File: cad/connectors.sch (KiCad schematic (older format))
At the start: 18 parts, among them J201 JACK_IN, J202 JACK_OUT, J203 CONN_PSU, J204 SW_BYPASS, J206 SW_FAT, K201 TQ2SA-5V, Q201 DTC123Y, U201 4013

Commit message: Placed components. Added possibility of having switches on connector board or circuit board.
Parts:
- added R204, R205: 150, Resistors_SMD:R_0805, symbol R
- C202: renamed from C?; value CP -> 10u; footprint (none) -> Capacitors_SMD:CP_Elec_4x4.5
- J205: renamed from J206; value SW_FAT -> SW_FAT_A; footprint Pin_Headers:Pin_Header_Straight_1x03_Pitch2.54mm -> flax_lib:SW_SPDT_through_hole
- J206: renamed from J?; footprint (none) -> flax_lib:SW_DPDT_through_hole
- J207, J208: renamed from J?; footprint (none) -> Pin_Headers:Pin_Header_Straight_1x06_Pitch2.54mm
- gave numbers to parts that had none: 1
- renumbered C201 to C203
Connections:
- wire segments 77 -> 79
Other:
- moved on the sheet: Q201
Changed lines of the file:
@@
 L DTC123Y Q201
 U 1 1 599C9C32
-P 5800 3800
-F 0 "Q201" H 6000 3875 50  0000 L CNN
-F 1 "DTC123Y" H 6000 3800 50  0000 L CNN
-F 2 "TO_SOT_Packages_SMD:SOT-23" H 5800 3800 50  0001 L CNN
-F 3 "" H 5800 3800 50  0001 L CNN
-	1    5800 3800
+P 5800 4200
+F 0 "Q201" H 6000 4275 50  0000 L CNN
+F 1 "DTC123Y" H 6000 4200 50  0000 L CNN
+F 2 "TO_SOT_Packages_SMD:SOT-23" H 5800 4200 50  0001 L CNN
+F 3 "" H 5800 4200 50  0001 L CNN
+	1    5800 4200
 	1    0    0    -1
 $EndComp
@@
 $EndComp
 $Comp
-L C C201
+L C C203
 U 1 1 599C9FED
 P 9800 950
-F 0 "C201" H 9825 1050 50  0000 L CNN
+F 0 "C203" H 9825 1050 50  0000 L CNN
 F 1 "100n" H 9825 850 50  0000 L CNN
 F 2 "Capacitors_SMD:C_0603" H 9838 800 50  0001 C CNN
@@
 $EndComp
 $Comp
-L GND #PWR218
+L GND #PWR01
 U 1 1 599D227D
 P 10400 2700
-F 0 "#PWR218" H 10400 2450 50  0001 C CNN
+F 0 "#PWR01" H 10400 2450 50  0001 C CNN
 F 1 "GND" H 10400 2550 50  0000 C CNN
 F 2 "" H 10400 2700 50  0001 C CNN
@@
 FX_OUT_A
 $Comp
-L VDD #PWR217
+L VDD #PWR02
 U 1 1 599D577B
 P 10400 2000
-F 0 "#PWR217" H 10400 1850 50  0001 C CNN
+F 0 "#PWR02" H 10400 1850 50  0001 C CNN
 F 1 "VDD" H 10400 2150 50  0000 C CNN
 F 2 "" H 10400 2000 50  0001 C CNN
@@
 $EndComp
 $Comp
-L VDD #PWR205
+L VDD #PWR03
 U 1 1 599D5C70
 P 1700 3900
-F 0 "#PWR205" H 1700 3750 50  0001 C CNN
+F 0 "#PWR03" H 1700 3750 50  0001 C CNN
 F 1 "VDD" H 1700 4050 50  0000 C CNN
 F 2 "" H 1700 3900 50  0001 C CNN
@@
 $EndComp
 $Comp
-L VSS #PWR201
+L VSS #PWR04
 U 1 1 599D5CD2
 P 1700 1100
-F 0 "#PWR201" H 1700 950 50  0001 C CNN
+F 0 "#PWR04" H 1700 950 50  0001 C CNN
 F 1 "VSS" H 1700 1250 50  0000 C CNN
 F 2 "" H 1700 1100 50  0001 C CNN
@@
 $EndComp
 $Comp
-L VDD #PWR215
+L VDD #PWR05
 U 1 1 599D63BF
 P 9800 700
-F 0 "#PWR215" H 9800 550 50  0001 C CNN
+F 0 "#PWR05" H 9800 550 50  0001 C CNN
 F 1 "VDD" H 9800 850 50  0000 C CNN
 F 2 "" H 9800 700 50  0001 C CNN
@@
 NoConn ~ 9400 1600
 $Comp
-L VSS #PWR216
+L VSS #PWR06
 U 1 1 599D692C
 P 9800 1200
-F 0 "#PWR216" H 9800 1050 50  0001 C CNN
+F 0 "#PWR06" H 9800 1050 50  0001 C CNN
 F 1 "VSS" H 9800 1350 50  0000 C CNN
 F 2 "" H 9800 1200 50  0001 C CNN
@@
 $EndComp
 $Comp
-L VSS #PWR213
+L VSS #PWR07
 U 1 1 599D6A53
 P 8800 800
-F 0 "#PWR213" H 8800 650 50  0001 C CNN
+F 0 "#PWR07" H 8800 650 50  0001 C CNN
 F 1 "VSS" H 8800 950 50  0000 C CNN
 F 2 "" H 8800 800 50  0001 C CNN
@@
 $EndComp
 $Comp
-L VDD #PWR214
+L VDD #PWR08
 U 1 1 599D6F63
 P 8800 2000
-F 0 "#PWR214" H 8800 1850 50  0001 C CNN
+F 0 "#PWR08" H 8800 1850 50  0001 C CNN
 F 1 "VDD" H 8800 2150 50  0000 C CNN
 F 2 "" H 8800 2000 50  0001 C CNN
@@
 NoConn ~ 8200 1200
 $Comp
-L VSS #PWR210
+L VSS #PWR09
 U 1 1 599DA718
 P 5700 800
-F 0 "#PWR210" H 5700 650 50  0001 C CNN
+F 0 "#PWR09" H 5700 650 50  0001 C CNN
 F 1 "VSS" H 5700 950 50  0000 C CNN
 F 2 "" H 5700 800 50  0001 C CNN
@@
 $EndComp
 $Comp
-L VSS #PWR211
+L VSS #PWR010
 U 1 1 599DA798
 P 5700 2000
-F 0 "#PWR211" H 5700 1850 50  0001 C CNN
+F 0 "#PWR010" H 5700 1850 50  0001 C CNN
 F 1 "VSS" H 5700 2150 50  0000 C CNN
 F 2 "" H 5700 2000 50  0001 C CNN
@@
 $EndComp
 $Comp
-L VSS #PWR208
+L VSS #PWR011
 U 1 1 599DB73B
 P 4900 2000
-F 0 "#PWR208" H 4900 1850 50  0001 C CNN
+F 0 "#PWR011" H 4900 1850 50  0001 C CNN
 F 1 "VSS" H 4900 2150 50  0000 C CNN
 F 2 "" H 4900 2000 50  0001 C CNN
@@
 $EndComp
 $Comp
-L VDD #PWR207
+L VDD #PWR012
 U 1 1 599DB9B0
 P 4200 1400
-F 0 "#PWR207" H 4200 1250 50  0001 C CNN
+F 0 "#PWR012" H 4200 1250 50  0001 C CNN
 F 1 "VDD" H 4200 1550 50  0000 C CNN
 F 2 "" H 4200 1400 50  0001 C CNN
@@
 Text Label 6400 1200 0    60   ~ 0
 BYPASS_CMD
-Text Label 5400 3800 2    60   ~ 0
+Text Label 5400 4200 2    60   ~ 0
 BYPASS_CMD
 Text Label 10300 2600 2    60   ~ 0
 BYPASS_CMD
 $Comp
-L +BATT #PWR209
+L +BATT #PWR013
 U 1 1 599DDDBD
-P 5500 3000
-F 0 "#PWR209" H 5500 2850 50  0001 C CNN
-F 1 "+BATT" H 5500 3140 50  0000 C CNN
-F 2 "" H 5500 3000 50  0001 C CNN
-F 3 "" H 5500 3000 50  0001 C CNN
-	1    5500 3000
+P 4900 3000
+F 0 "#PWR013" H 4900 2850 50  0001 C CNN
+F 1 "+BATT" H 4900 3140 50  0000 C CNN
+F 2 "" H 4900 3000 50  0001 C CNN
+F 3 "" H 4900 3000 50  0001 C CNN
+	1    4900 3000
 	0    -1   -1   0
 $EndComp
@@
 AUDIO_OUT
 $Comp
-L CONN_01X03 J206
+L CONN_01X03 J205
 U 1 1 599E0F67
 P 8000 2700
-F 0 "J206" H 8000 2900 50  0000 C CNN
-F 1 "SW_FAT" V 8100 2700 50  0000 C CNN
-F 2 "Pin_Headers:Pin_Header_Straight_1x03_Pitch2.54mm" H 8000 2700 50  0001 C CNN
+F 0 "J205" H 8000 2900 50  0000 C CNN
+F 1 "SW_FAT_A" V 8100 2700 50  0000 C CNN
+F 2 "flax_lib:SW_SPDT_through_hole" H 8000 2700 50  0001 C CNN
 F 3 "" H 8000 2700 50  0001 C CNN
 	1    8000 2700
@@
 NoConn ~ 1600 2300
 $Comp
-L +BATT #PWR204
+L +BATT #PWR014
 U 1 1 599E2D1E
 P 1700 3800
-F 0 "#PWR204" H 1700 3650 50  0001 C CNN
+F 0 "#PWR014" H 1700 3650 50  0001 C CNN
 F 1 "+BATT" H 1700 3940 50  0000 C CNN
 F 2 "" H 1700 3800 50  0001 C CNN
@@
 $EndComp
 $Comp
-L VSS #PWR212
+L VSS #PWR015
 U 1 1 599E3B90
-P 5900 4100
-F 0 "#PWR212" H 5900 3950 50  0001 C CNN
-F 1 "VSS" H 5900 4250 50  0000 C CNN
-F 2 "" H 5900 4100 50  0001 C CNN
-F 3 "" H 5900 4100 50  0001 C CNN
-	1    5900 4100
+P 5900 4500
+F 0 "#PWR015" H 5900 4350 50  0001 C CNN
+F 1 "VSS" H 5900 4650 50  0000 C CNN
+F 2 "" H 5900 4500 50  0001 C CNN
+F 3 "" H 5900 4500 50  0001 C CNN
+	1    5900 4500
 	-1   0    0    1
 $EndComp
@@
 NoConn ~ 1600 1200
 $Comp
-L VSS #PWR202
+L VSS #PWR016
 U 1 1 599E4020
 P 1700 1900
-F 0 "#PWR202" H 1700 1750 50  0001 C CNN
+F 0 "#PWR016" H 1700 1750 50  0001 C CNN
 F 1 "VSS" H 1700 2050 50  0000 C CNN
 F 2 "" H 1700 1900 50  0001 C CNN
@@
 $EndComp
 $Comp
-L VSS #PWR203
+L VSS #PWR017
 U 1 1 599E457A
 P 1700 3700
-F 0 "#PWR203" H 1700 3550 50  0001 C CNN
+F 0 "#PWR017" H 1700 3550 50  0001 C CNN
 F 1 "VSS" H 1700 3850 50  0000 C CNN
 F 2 "" H 1700 3700 50  0001 C CNN
@@
 Connection ~ 5900 3500
 Wire Wire Line
-	5900 4000 5900 4100
-Wire Wire Line
-	5550 3800 4800 3800
+	5900 4400 5900 4500
+Wire Wire Line
+	5550 4200 4800 4200
 Wire Wire Line
 	6400 1600 6300 1600
@@
 	6300 1200 7000 1200
 Wire Wire Line
-	5500 3000 5700 3000
+	5300 3000 5700 3000
 Wire Wire Line
 	5700 3000 5700 3100
@@
 	2200 1300 2200 1400
 $Comp
-L VSS #PWR206
+L VSS #PWR018
 U 1 1 59A2E46C
 P 2200 1800
-F 0 "#PWR206" H 2200 1650 50  0001 C CNN
+F 0 "#PWR018" H 2200 1650 50  0001 C CNN
 F 1 "VSS" H 2200 1950 50  0000 C CNN
 F 2 "" H 2200 1800 50  0001 C CNN
@@
 Connection ~ 1650 1900
 $Comp
-L C C?
+L C C201
 U 1 1 59A4C299
 P 7650 2500
-F 0 "C?" H 7675 2600 50  0000 L CNN
+F 0 "C201" H 7675 2600 50  0000 L CNN
 F 1 "100n" H 7675 2400 50  0000 L CNN
 F 2 "Capacitors_SMD:C_0603" H 7688 2350 50  0001 C CNN
@@
 	7400 2500 7500 2500
 $Comp
-L CP C?
+L CP C202
 U 1 1 59A4C4B8
 P 7650 2900
-F 0 "C?" H 7675 3000 50  0000 L CNN
-F 1 "CP" H 7675 2800 50  0000 L CNN
-F 2 "" H 7688 2750 50  0001 C CNN
+F 0 "C202" H 7675 3000 50  0000 L CNN
+F 1 "10u" H 7675 2800 50  0000 L CNN
+F 2 "Capacitors_SMD:CP_Elec_4x4.5" H 7688 2750 50  0001 C CNN
 F 3 "" H 7650 2900 50  0001 C CNN
 	1    7650 2900
@@
 FX_IN_A
 $Comp
-L CONN_01X06 J?
+L CONN_01X06 J207
 U 1 1 59A4F4ED
 P 10700 2350
-F 0 "J?" H 10700 2700 50  0000 C CNN
+F 0 "J207" H 10700 2700 50  0000 C CNN
 F 1 "CONN_SIGNALS_A" V 10800 2350 50  0000 C CNN
-F 2 "" H 10700 2350 50  0001 C CNN
+F 2 "Pin_Headers:Pin_Header_Straight_1x06_Pitch2.54mm" H 10700 2350 50  0001 C CNN
 F 3 "" H 10700 2350 50  0001 C CNN
 	1    10700 2350
@@
 EQ_SW_1_1B
 $Comp
-L CONN_01X06 J?
+L CONN_01X06 J208
 U 1 1 59A529D0
 P 10700 3450
-F 0 "J?" H 10700 3800 50  0000 C CNN
+F 0 "J208" H 10700 3800 50  0000 C CNN
 F 1 "CONN_SW_EQ_A" V 10800 3450 50  0000 C CNN
-F 2 "" H 10700 3450 50  0001 C CNN
+F 2 "Pin_Headers:Pin_Header_Straight_1x06_Pitch2.54mm" H 10700 3450 50  0001 C CNN
 F 3 "" H 10700 3450 50  0001 C CNN
 	1    10700 3450
@@
 	9700 3700 10500 3700
 $Comp
-L CONN_02X03 J?
+L CONN_02X03 J206
 U 1 1 59A53228
 P 8050 3700
-F 0 "J?" H 8050 3900 50  0000 C CNN
+F 0 "J206" H 8050 3900 50  0000 C CNN
 F 1 "SW_EQ_A" H 8050 3500 50  0000 C CNN
-F 2 "" H 8050 2500 50  0001 C CNN
+F 2 "flax_lib:SW_DPDT_through_hole" H 8050 2500 50  0001 C CNN
 F 3 "" H 8050 2500 50  0001 C CNN
 	1    8050 3700
@@
 Wire Wire Line
 	8300 3800 9000 3800
+$Comp
+L R R204
+U 1 1 59A553B7
+P 5150 3000
+F 0 "R204" V 5230 3000 50  0000 C CNN
+F 1 "150" V 5150 3000 50  0000 C CNN
+F 2 "Resistors_SMD:R_0805" V 5080 3000 50  0001 C CNN
+F 3 "" H 5150 3000 50  0001 C CNN
+	1    5150 3000
+	0    -1   -1   0
+$EndComp
+Wire Wire Line
+	5000 3000 4900 3000
+$Comp
+L R R205
+U 1 1 59A55A74
+P 5900 3750
+F 0 "R205" V 5980 3750 50  0000 C CNN
+F 1 "150" V 5900 3750 50  0000 C CNN
+F 2 "Resistors_SMD:R_0805" V 5830 3750 50  0001 C CNN
+F 3 "" H 5900 3750 50  0001 C CNN
+	1    5900 3750
+	1    0    0    -1
+$EndComp
+Wire Wire Line
+	5900 3900 5900 4000
 $EndSCHEMATC

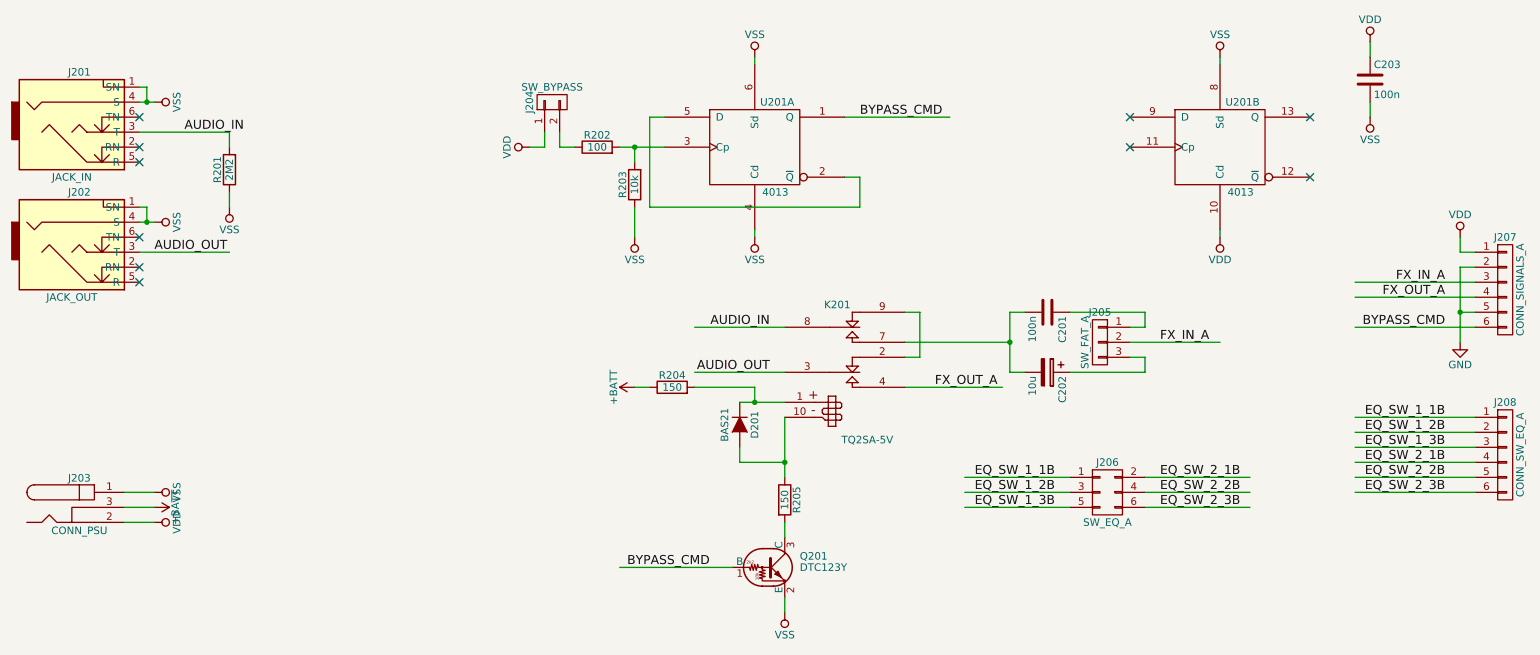
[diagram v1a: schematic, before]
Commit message: Corrected pots orientation.
Finished layout.
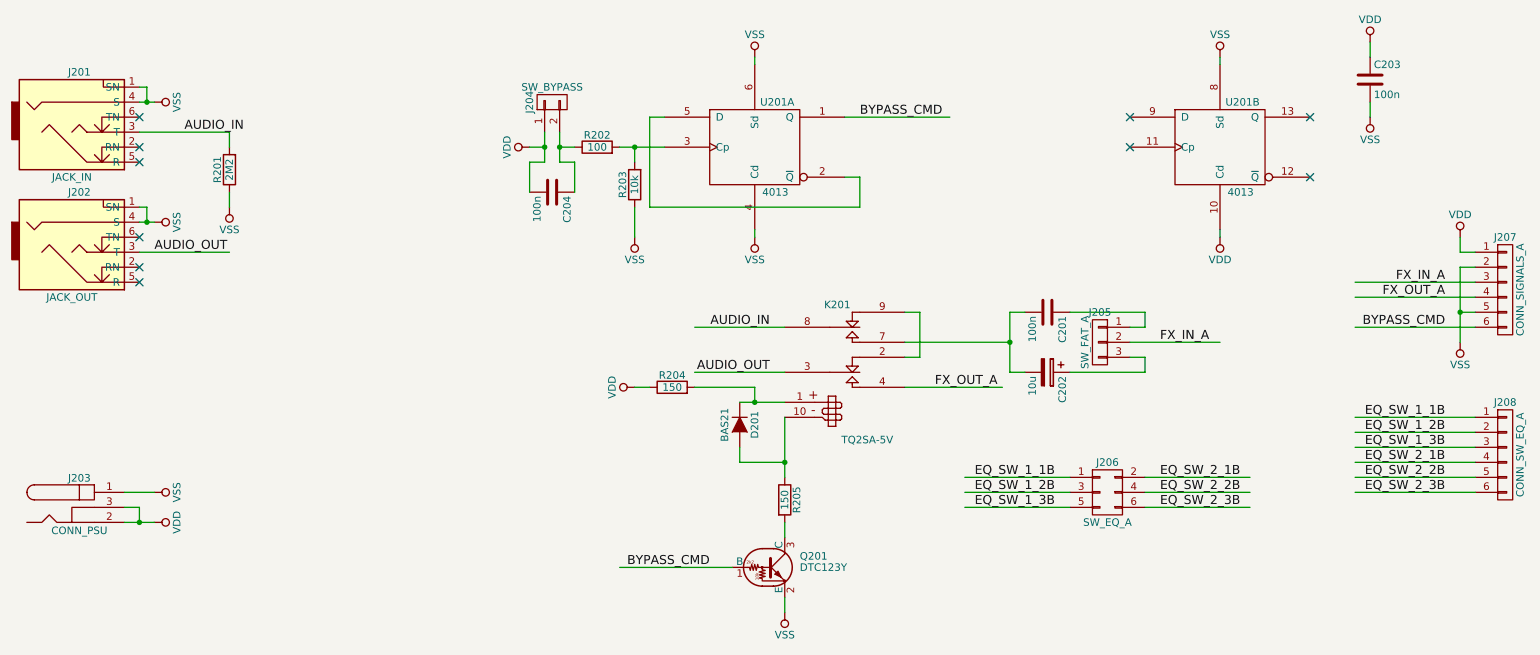
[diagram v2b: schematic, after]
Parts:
- added C204: 100n, Capacitors_SMD:C_0603, symbol C
- J207, J208: footprint Pin_Headers:Pin_Header_Straight_1x06_Pitch2.54mm -> Pin_Headers:Pin_Header_Straight_1x06_Pitch1.27mm
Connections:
- net labels removed: +BATT, GND
- wire segments 79 -> 84
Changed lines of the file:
@@
 LIBS:contrib
 LIBS:valves
-LIBS:flax_lib
 LIBS:hot_silicon_fuzz-cache
 EELAYER 25 0
@@
 	1    0    0    -1
 $EndComp
-$Comp
-L GND #PWR01
-U 1 1 599D227D
-P 10400 2700
-F 0 "#PWR01" H 10400 2450 50  0001 C CNN
-F 1 "GND" H 10400 2550 50  0000 C CNN
-F 2 "" H 10400 2700 50  0001 C CNN
-F 3 "" H 10400 2700 50  0001 C CNN
-	1    10400 2700
-	1    0    0    -1
-$EndComp
 Text Label 10300 2400 2    60   ~ 0
 FX_OUT_A
 $Comp
-L VDD #PWR02
+L VDD #PWR01
 U 1 1 599D577B
 P 10400 2000
-F 0 "#PWR02" H 10400 1850 50  0001 C CNN
+F 0 "#PWR01" H 10400 1850 50  0001 C CNN
 F 1 "VDD" H 10400 2150 50  0000 C CNN
 F 2 "" H 10400 2000 50  0001 C CNN
@@
 $EndComp
 $Comp
-L VDD #PWR03
+L VDD #PWR02
 U 1 1 599D5C70
 P 1700 3900
-F 0 "#PWR03" H 1700 3750 50  0001 C CNN
+F 0 "#PWR02" H 1700 3750 50  0001 C CNN
 F 1 "VDD" H 1700 4050 50  0000 C CNN
 F 2 "" H 1700 3900 50  0001 C CNN
@@
 $EndComp
 $Comp
-L VSS #PWR04
+L VSS #PWR03
 U 1 1 599D5CD2
 P 1700 1100
-F 0 "#PWR04" H 1700 950 50  0001 C CNN
+F 0 "#PWR03" H 1700 950 50  0001 C CNN
 F 1 "VSS" H 1700 1250 50  0000 C CNN
 F 2 "" H 1700 1100 50  0001 C CNN
@@
 $EndComp
 $Comp
-L VDD #PWR05
+L VDD #PWR04
 U 1 1 599D63BF
 P 9800 700
-F 0 "#PWR05" H 9800 550 50  0001 C CNN
+F 0 "#PWR04" H 9800 550 50  0001 C CNN
 F 1 "VDD" H 9800 850 50  0000 C CNN
 F 2 "" H 9800 700 50  0001 C CNN
@@
 NoConn ~ 9400 1600
 $Comp
-L VSS #PWR06
+L VSS #PWR05
 U 1 1 599D692C
 P 9800 1200
-F 0 "#PWR06" H 9800 1050 50  0001 C CNN
+F 0 "#PWR05" H 9800 1050 50  0001 C CNN
 F 1 "VSS" H 9800 1350 50  0000 C CNN
 F 2 "" H 9800 1200 50  0001 C CNN
@@
 $EndComp
 $Comp
-L VSS #PWR07
+L VSS #PWR06
 U 1 1 599D6A53
 P 8800 800
-F 0 "#PWR07" H 8800 650 50  0001 C CNN
+F 0 "#PWR06" H 8800 650 50  0001 C CNN
 F 1 "VSS" H 8800 950 50  0000 C CNN
 F 2 "" H 8800 800 50  0001 C CNN
@@
 $EndComp
 $Comp
-L VDD #PWR08
+L VDD #PWR07
 U 1 1 599D6F63
 P 8800 2000
-F 0 "#PWR08" H 8800 1850 50  0001 C CNN
+F 0 "#PWR07" H 8800 1850 50  0001 C CNN
 F 1 "VDD" H 8800 2150 50  0000 C CNN
 F 2 "" H 8800 2000 50  0001 C CNN
@@
 NoConn ~ 8200 1200
 $Comp
-L VSS #PWR09
+L VSS #PWR08
 U 1 1 599DA718
 P 5700 800
-F 0 "#PWR09" H 5700 650 50  0001 C CNN
+F 0 "#PWR08" H 5700 650 50  0001 C CNN
 F 1 "VSS" H 5700 950 50  0000 C CNN
 F 2 "" H 5700 800 50  0001 C CNN
@@
 $EndComp
 $Comp
-L VSS #PWR010
+L VSS #PWR09
 U 1 1 599DA798
 P 5700 2000
-F 0 "#PWR010" H 5700 1850 50  0001 C CNN
+F 0 "#PWR09" H 5700 1850 50  0001 C CNN
 F 1 "VSS" H 5700 2150 50  0000 C CNN
 F 2 "" H 5700 2000 50  0001 C CNN
@@
 $EndComp
 $Comp
-L VSS #PWR011
+L VSS #PWR010
 U 1 1 599DB73B
 P 4900 2000
-F 0 "#PWR011" H 4900 1850 50  0001 C CNN
+F 0 "#PWR010" H 4900 1850 50  0001 C CNN
 F 1 "VSS" H 4900 2150 50  0000 C CNN
 F 2 "" H 4900 2000 50  0001 C CNN
@@
 $EndComp
 $Comp
-L VDD #PWR012
+L VDD #PWR011
 U 1 1 599DB9B0
 P 4200 1400
-F 0 "#PWR012" H 4200 1250 50  0001 C CNN
+F 0 "#PWR011" H 4200 1250 50  0001 C CNN
 F 1 "VDD" H 4200 1550 50  0000 C CNN
 F 2 "" H 4200 1400 50  0001 C CNN
@@
 Text Label 10300 2600 2    60   ~ 0
 BYPASS_CMD
-$Comp
-L +BATT #PWR013
-U 1 1 599DDDBD
-P 4900 3000
-F 0 "#PWR013" H 4900 2850 50  0001 C CNN
-F 1 "+BATT" H 4900 3140 50  0000 C CNN
-F 2 "" H 4900 3000 50  0001 C CNN
-F 3 "" H 4900 3000 50  0001 C CNN
-	1    4900 3000
-	0    -1   -1   0
-$EndComp
 Text Label 8400 2700 0    60   ~ 0
 FX_IN_A
@@
 NoConn ~ 1600 2300
 $Comp
-L +BATT #PWR014
-U 1 1 599E2D1E
-P 1700 3800
-F 0 "#PWR014" H 1700 3650 50  0001 C CNN
-F 1 "+BATT" H 1700 3940 50  0000 C CNN
-F 2 "" H 1700 3800 50  0001 C CNN
-F 3 "" H 1700 3800 50  0001 C CNN
-	1    1700 3800
-	0    1    1    0
-$EndComp
-$Comp
-L VSS #PWR015
+L VSS #PWR012
 U 1 1 599E3B90
 P 5900 4500
-F 0 "#PWR015" H 5900 4350 50  0001 C CNN
+F 0 "#PWR012" H 5900 4350 50  0001 C CNN
 F 1 "VSS" H 5900 4650 50  0000 C CNN
 F 2 "" H 5900 4500 50  0001 C CNN
@@
 NoConn ~ 1600 1200
 $Comp
-L VSS #PWR016
+L VSS #PWR013
 U 1 1 599E4020
 P 1700 1900
-F 0 "#PWR016" H 1700 1750 50  0001 C CNN
+F 0 "#PWR013" H 1700 1750 50  0001 C CNN
 F 1 "VSS" H 1700 2050 50  0000 C CNN
 F 2 "" H 1700 1900 50  0001 C CNN
@@
 $EndComp
 $Comp
-L VSS #PWR017
+L VSS #PWR014
 U 1 1 599E457A
 P 1700 3700
-F 0 "#PWR017" H 1700 3550 50  0001 C CNN
+F 0 "#PWR014" H 1700 3550 50  0001 C CNN
 F 1 "VSS" H 1700 3850 50  0000 C CNN
 F 2 "" H 1700 3700 50  0001 C CNN
@@
 	4900 1800 4900 2000
 Wire Wire Line
-	4400 1300 4400 1400
+	4400 1300 4400 1500
 Wire Wire Line
 	4400 1400 4500 1400
@@
 	4200 1400 4300 1400
 Wire Wire Line
-	4300 1400 4300 1300
+	4300 1300 4300 1500
 Wire Wire Line
 	5600 3100 5900 3100
@@
 Wire Wire Line
 	1700 1900 1600 1900
-Wire Wire Line
-	1700 3800 1500 3800
 Wire Wire Line
 	1700 1100 1600 1100
@@
 	2200 1300 2200 1400
 $Comp
-L VSS #PWR018
+L VSS #PWR015
 U 1 1 59A2E46C
 P 2200 1800
-F 0 "#PWR018" H 2200 1650 50  0001 C CNN
+F 0 "#PWR015" H 2200 1650 50  0001 C CNN
 F 1 "VSS" H 2200 1950 50  0000 C CNN
 F 2 "" H 2200 1800 50  0001 C CNN
@@
 F 0 "J207" H 10700 2700 50  0000 C CNN
 F 1 "CONN_SIGNALS_A" V 10800 2350 50  0000 C CNN
-F 2 "Pin_Headers:Pin_Header_Straight_1x06_Pitch2.54mm" H 10700 2350 50  0001 C CNN
+F 2 "Pin_Headers:Pin_Header_Straight_1x06_Pitch1.27mm" H 10700 2350 50  0001 C CNN
 F 3 "" H 10700 2350 50  0001 C CNN
 	1    10700 2350
@@
 F 0 "J208" H 10700 3800 50  0000 C CNN
 F 1 "CONN_SW_EQ_A" V 10800 3450 50  0000 C CNN
-F 2 "Pin_Headers:Pin_Header_Straight_1x06_Pitch2.54mm" H 10700 3450 50  0001 C CNN
+F 2 "Pin_Headers:Pin_Header_Straight_1x06_Pitch1.27mm" H 10700 3450 50  0001 C CNN
 F 3 "" H 10700 3450 50  0001 C CNN
 	1    10700 3450
@@
 Wire Wire Line
 	5900 3900 5900 4000
+Wire Wire Line
+	1500 3800 1600 3800
+Wire Wire Line
+	1600 3800 1600 3900
+Connection ~ 1600 3900
+$Comp
+L VDD #PWR016
+U 1 1 59A8681E
+P 4900 3000
+F 0 "#PWR016" H 4900 2850 50  0001 C CNN
+F 1 "VDD" H 4900 3150 50  0000 C CNN
+F 2 "" H 4900 3000 50  0001 C CNN
+F 3 "" H 4900 3000 50  0001 C CNN
+	1    4900 3000
+	0    -1   -1   0
+$EndComp
+$Comp
+L C C204
+U 1 1 59A876F8
+P 4350 1700
+F 0 "C204" H 4375 1800 50  0000 L CNN
+F 1 "100n" H 4375 1600 50  0000 L CNN
+F 2 "Capacitors_SMD:C_0603" H 4388 1550 50  0001 C CNN
+F 3 "" H 4350 1700 50  0001 C CNN
+	1    4350 1700
+	0    1    1    0
+$EndComp
+Wire Wire Line
+	4400 1500 4500 1500
+Wire Wire Line
+	4500 1500 4500 1700
+Connection ~ 4400 1400
+Wire Wire Line
+	4200 1700 4200 1500
+Wire Wire Line
+	4200 1500 4300 1500
+Connection ~ 4300 1400
+$Comp
+L VSS #PWR017
+U 1 1 59A886A7
+P 10400 2700
+F 0 "#PWR017" H 10400 2550 50  0001 C CNN
+F 1 "VSS" H 10400 2850 50  0000 C CNN
+F 2 "" H 10400 2700 50  0001 C CNN
+F 3 "" H 10400 2700 50  0001 C CNN
+	1    10400 2700
+	-1   0    0    1
+$EndComp
 $EndSCHEMATC
